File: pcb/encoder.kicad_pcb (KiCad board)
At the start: 2 copper layers, 65 x 56 mm, 7 parts, among them J1 GPIO

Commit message: snapshot...working on routing
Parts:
- added C1: 0.1uF, Capacitor_SMD:C_0603_1608Metric, F.Cu at (139.7, 59.0)
- added C2: 0.1uF, Capacitor_SMD:C_0603_1608Metric, F.Cu at (139.7, 74.5)
- added C3: 10uF, Capacitor_SMD:C_0805_2012Metric, F.Cu at (108.5, 53.0)
- added J2: Foot Switch, TerminalBlock_Phoenix:TerminalBlock_Phoenix_PT-1,5-4-5.0-H_1x04_P5.00mm_Horizontal, F.Cu at (157.5, 68.5)
- added J3: X, TerminalBlock_Phoenix:TerminalBlock_Phoenix_PT-1,5-4-5.0-H_1x04_P5.00mm_Horizontal, F.Cu at (113.0, 64.5)
- added J4: X', TerminalBlock_Phoenix:TerminalBlock_Phoenix_PT-1,5-4-5.0-H_1x04_P5.00mm_Horizontal, F.Cu at (157.5, 90.5)
- added J5: Y, TerminalBlock_Phoenix:TerminalBlock_Phoenix_PT-1,5-4-5.0-H_1x04_P5.00mm_Horizontal, F.Cu at (111.0, 91.5)
- added J6: Z, TerminalBlock_Phoenix:TerminalBlock_Phoenix_PT-1,5-4-5.0-H_1x04_P5.00mm_Horizontal, F.Cu at (133.0, 91.5)
- added R1: 4.7K, Resistor_SMD:R_0603_1608Metric, F.Cu at (150.7, 57.0)
- added R2: 4.7K, Resistor_SMD:R_0603_1608Metric, F.Cu at (128.2, 64.5)
- added R3: 4.7K, Resistor_SMD:R_0603_1608Metric, F.Cu at (128.2, 66.0)
- added R4: 4.7K, Resistor_SMD:R_0603_1608Metric, F.Cu at (128.2, 79.5)
- added R5: 4.7K, Resistor_SMD:R_0603_1608Metric, F.Cu at (128.2, 81.0)
- added R6: 4.7K, Resistor_SMD:R_0603_1608Metric, F.Cu at (139.7, 65.5)
- added R7: 4.7K, Resistor_SMD:R_0603_1608Metric, F.Cu at (139.7, 64.0)
- added R8: 4.7K, Resistor_SMD:R_0603_1608Metric, F.Cu at (139.7, 79.5)
- added R9: 4.7K, Resistor_SMD:R_0603_1608Metric, F.Cu at (139.7, 81.0)
- moved LS7466-S2 15.8 mm to (134.0, 78.9)
- moved LS7466-S1 10.1 mm to (134.0, 63.5)
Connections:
- LS7466-S1 pad 11: unconnected-(LS7466-S1-Ay-Pad11) -> Net-(J4-Pin_2)
- LS7466-S1 pad 12: unconnected-(LS7466-S1-By-Pad12) -> Net-(J4-Pin_3)
- LS7466-S1 pad 13: unconnected-(LS7466-S1-Zy-Pad13) -> GND
- LS7466-S1 pad 14: unconnected-(LS7466-S1-CEy-Pad14) -> +3.3V
- LS7466-S1 pad 16: unconnected-(LS7466-S1-VDD-Pad16) -> +3.3V
- LS7466-S1 pad 5: unconnected-(LS7466-S1-Ax-Pad5) -> Net-(J3-Pin_2)
- LS7466-S1 pad 6: unconnected-(LS7466-S1-Bx-Pad6) -> Net-(J3-Pin_3)
- LS7466-S1 pad 7: unconnected-(LS7466-S1-Zx-Pad7) -> GND
- LS7466-S1 pad 8: unconnected-(LS7466-S1-GND-Pad8) -> GND
- LS7466-S1 pad 9: unconnected-(LS7466-S1-CEx-Pad9) -> +3.3V
- LS7466-S2 pad 11: unconnected-(LS7466-S2-Ay-Pad11) -> Net-(J6-Pin_2)
- LS7466-S2 pad 12: unconnected-(LS7466-S2-By-Pad12) -> Net-(J6-Pin_3)
- LS7466-S2 pad 13: unconnected-(LS7466-S2-Zy-Pad13) -> GND
- LS7466-S2 pad 14: unconnected-(LS7466-S2-CEy-Pad14) -> +3.3V
- LS7466-S2 pad 16: unconnected-(LS7466-S2-VDD-Pad16) -> +3.3V
- LS7466-S2 pad 5: unconnected-(LS7466-S2-Ax-Pad5) -> Net-(J5-Pin_2)
- LS7466-S2 pad 6: unconnected-(LS7466-S2-Bx-Pad6) -> Net-(J5-Pin_3)
- LS7466-S2 pad 7: unconnected-(LS7466-S2-Zx-Pad7) -> GND
- LS7466-S2 pad 8: unconnected-(LS7466-S2-GND-Pad8) -> GND
- LS7466-S2 pad 9: unconnected-(LS7466-S2-CEx-Pad9) -> +3.3V
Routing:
- net GND: track 0.00 -> 226.8 mm, vias 0 -> 4
- net +3.3V: track 0.00 -> 72.1 mm
- net /GPIO9/SPI0.MISO: track 0.00 -> 48.3 mm
- net /GPIO10/SPI0.MOSI: track 0.00 -> 48.0 mm
- net /GPIO11/SPI0.SCLK: track 0.00 -> 47.9 mm
- net /GPIO8/SPI0.CE0: track 0.00 -> 36.7 mm
- net /GPIO7/SPI0.CE1: track 0.00 -> 22.1 mm
- net Net-(J5-Pin_2): track 0.00 -> 21.1 mm
- net /GPIO26: track 0.00 -> 18.3 mm
- net Net-(J5-Pin_3): track 0.00 -> 16.4 mm
- net Net-(J6-Pin_3): track 0.00 -> 16.1 mm
- net Net-(J6-Pin_2): track 0.00 -> 13.3 mm
- net Net-(J3-Pin_3): track 0.00 -> 2.77 mm
- net Net-(J3-Pin_2): track 0.00 -> 2.68 mm
- net +5V: track 0.00 -> 2.54 mm
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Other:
- outline, holes or cut-outs redrawn
- board text removed: "CAMERA (OPTIONAL)"
- board text removed: "DISPLAY (OPTIONAL)"
- board text removed: "PoE"

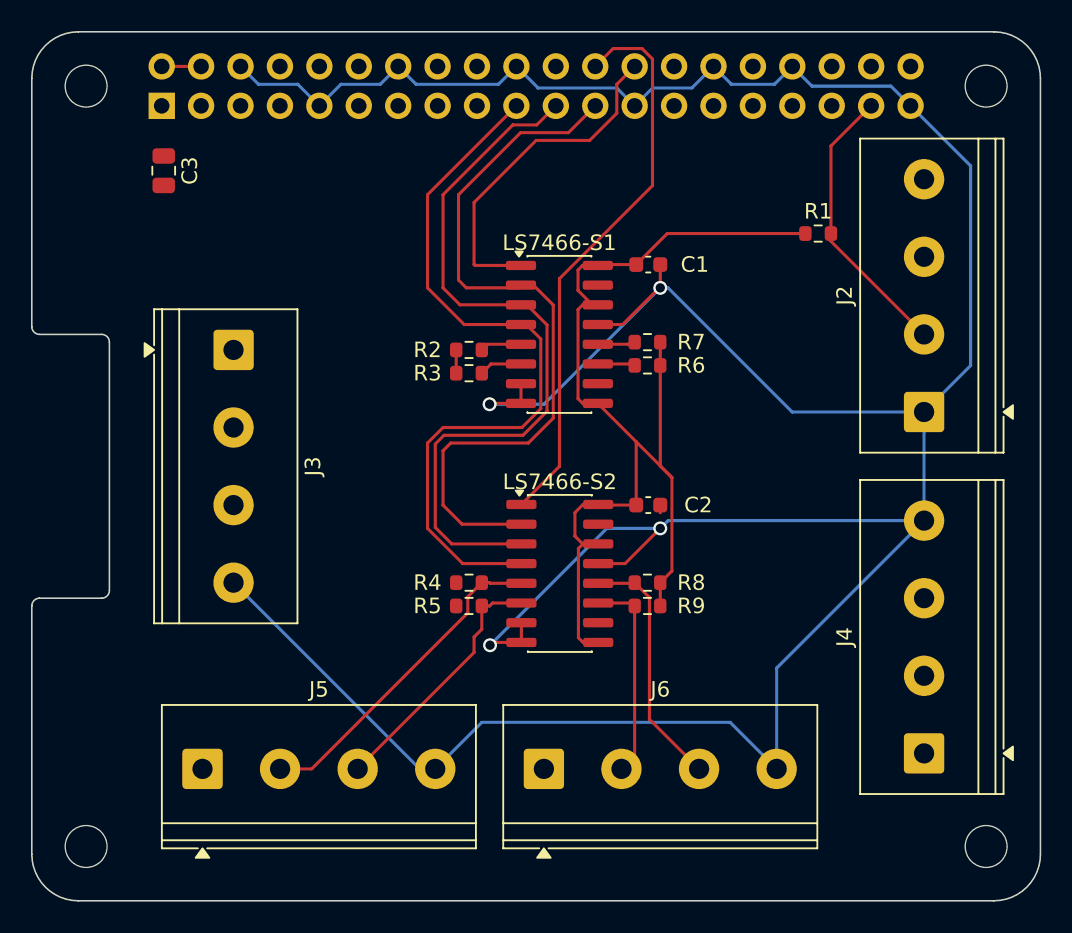
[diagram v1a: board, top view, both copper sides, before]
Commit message: route with ls74633 chips
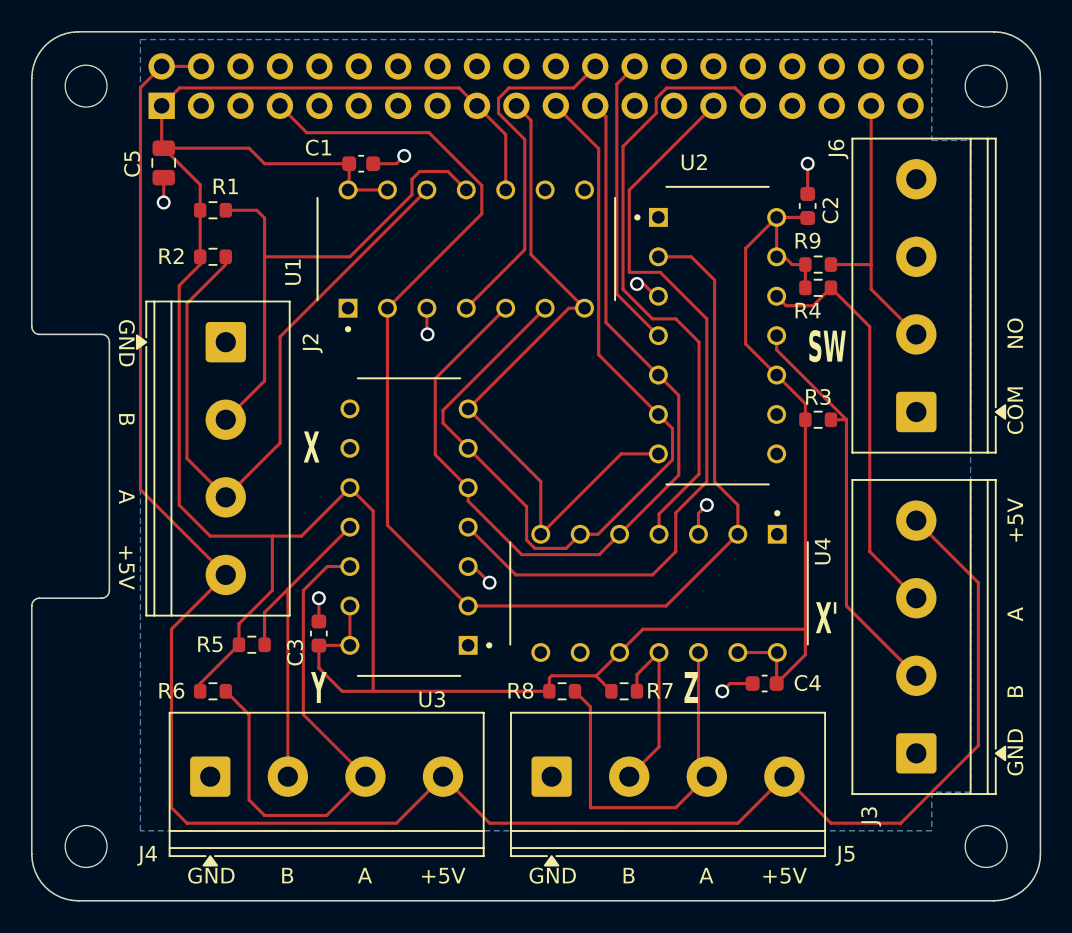
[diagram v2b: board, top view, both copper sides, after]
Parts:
- removed LS7466-S1, LS7466-S2: ~, Package_SO:SOIC-16_3.9x9.9mm_P1.27mm
- added C4: 0.1uF, Capacitor_SMD:C_0603_1608Metric, F.Cu at (147.2, 86.0)
- added C5: 10uF, Capacitor_SMD:C_0805_2012Metric, F.Cu at (108.5, 52.5)
- added U1: LS7366R, LS7366R:DIP762W45P254L1917H533Q14, F.Cu at (128.0, 58.0)
- added U2: LS7366R, LS7366R:DIP762W45P254L1917H533Q14, F.Cu at (144.2, 63.6)
- added U3: LS7366R, LS7366R:DIP762W45P254L1917H533Q14, F.Cu at (124.3, 75.9)
- added U4: LS7366R, LS7366R:DIP762W45P254L1917H533Q14, F.Cu at (140.4, 80.2)
- C3: value 10uF -> 0.1uF; footprint Capacitor_SMD:C_0805_2012Metric -> Capacitor_SMD:C_0603_1608Metric
- J2: value Foot Switch -> X
- J3: value X -> X'
- J4: value X' -> Y
- J5: value Y -> Z
- J6: value Z -> Foot Switch
- moved J3 51.1 mm to (157.0, 90.5), turned to 90 degrees
- moved J4 46.0 mm to (111.5, 92.0), turned to 0 degrees
- moved J2 45.2 mm to (112.5, 64.0), turned to -90 degrees
- moved R1 39.0 mm to (111.7, 55.5)
- moved R6 35.0 mm to (111.7, 86.5), turned to 0 degrees
- moved J6 33.2 mm to (157.0, 68.5), turned to 90 degrees
- moved C3 31.5 mm to (118.5, 82.8), turned to 90 degrees
- moved R4 29.4 mm to (150.7, 60.5)
- moved R9 24.6 mm to (150.7, 59.0), turned to 0 degrees
- moved R3 22.7 mm to (150.7, 69.0)
- moved R7 22.5 mm to (138.2, 86.5), turned to 0 degrees
- moved J5 22.5 mm to (133.5, 92.0)
- moved C2 21.8 mm to (150.0, 55.2), turned to 90 degrees
- moved C1 19.6 mm to (121.2, 52.5)
- moved R2 17.6 mm to (111.7, 58.5)
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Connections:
- C3 pad 1: +3V3 -> +3.3V
- J1 pad 1: +3V3 -> +3.3V
- J1 pad 17: +3V3 -> +3.3V
- J2 pad 2: /GPIO26 -> Net-(J2-Pin_2)
- J2 pad 3: unconnected-(J2-Pin_3-Pad3) -> Net-(J2-Pin_3)
- J2 pad 4: unconnected-(J2-Pin_4-Pad4) -> +5V
- J6 pad 1: +5V -> GND
- J6 pad 2: Net-(J6-Pin_2) -> /GPIO26
- J6 pad 3: Net-(J6-Pin_3) -> unconnected-(J6-Pin_3-Pad3)
- J6 pad 4: GND -> unconnected-(J6-Pin_4-Pad4)
- R1 pad 2: /GPIO26 -> Net-(J2-Pin_2)
- R2 pad 2: Net-(J3-Pin_2) -> Net-(J2-Pin_3)
- R3 pad 2: Net-(J3-Pin_3) -> Net-(J3-Pin_2)
- R4 pad 2: Net-(J5-Pin_2) -> Net-(J3-Pin_3)
- R5 pad 2: Net-(J5-Pin_3) -> Net-(J4-Pin_2)
- R6 pad 2: Net-(J4-Pin_2) -> Net-(J4-Pin_3)
- R7 pad 2: Net-(J4-Pin_3) -> Net-(J5-Pin_2)
- R8 pad 2: Net-(J6-Pin_3) -> Net-(J5-Pin_3)
- R9 pad 2: Net-(J6-Pin_2) -> /GPIO26
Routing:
- net GND: track 226.8 -> 16.7 mm, vias 4 -> 9
- net +5V: track 2.54 -> 130.2 mm
- net +3.3V: track 72.1 -> 197.6 mm
- net /GPIO4/GPCLK0: track 0.00 -> 87.4 mm
- net /GPIO5: track 0.00 -> 50.3 mm
- net Net-(J2-Pin_3): track 0.00 -> 42.2 mm
- net /GPIO6: track 0.00 -> 39.9 mm
- net Net-(J2-Pin_2): track 0.00 -> 33.1 mm
- net Net-(J4-Pin_3): track 1.93 -> 33.9 mm
- net Net-(J3-Pin_2): track 2.68 -> 26.6 mm
- net Net-(J3-Pin_3): track 2.77 -> 26.5 mm
- net Net-(J4-Pin_2): track 2.14 -> 21.9 mm
- net Net-(J6-Pin_3): track 16.1 -> 0.00 mm
- net /GPIO8/SPI0.CE0: track 36.7 -> 22.9 mm
- net Net-(J6-Pin_2): track 13.3 -> 0.00 mm
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- added copper zone on B.Cu, net GND
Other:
- board text added: "+5V"
- board text added: "A"
- board text added: "B"
- board text added: "COM"
- board text added: "GND"
- board text added: "NO"
- board text added: "SW"
- board text added: "X"
- board text added: "X'"
- board text added: "Y"
- board text added: "Z"

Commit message: update hardware.md to match schematic
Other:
- board text added: "https://github.com/scottfeldman/closinuf"
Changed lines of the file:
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@@
+		)
+	)
+	(gr_text "https://github.com/scottfeldman/closinuf"
+		(at 148.5 89 0)
+		(layer "B.SilkS")
+		(effects
+			(font
+				(size 1 1)
+				(thickness 0.15)
+			)
+			(justify left bottom mirror)
 		)
 	)

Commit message: update BOM
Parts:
- moved C4 1.55 mm to (148.8, 86.0), turned to 0 degrees
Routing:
- net GND: track 16.7 -> 16.0 mm

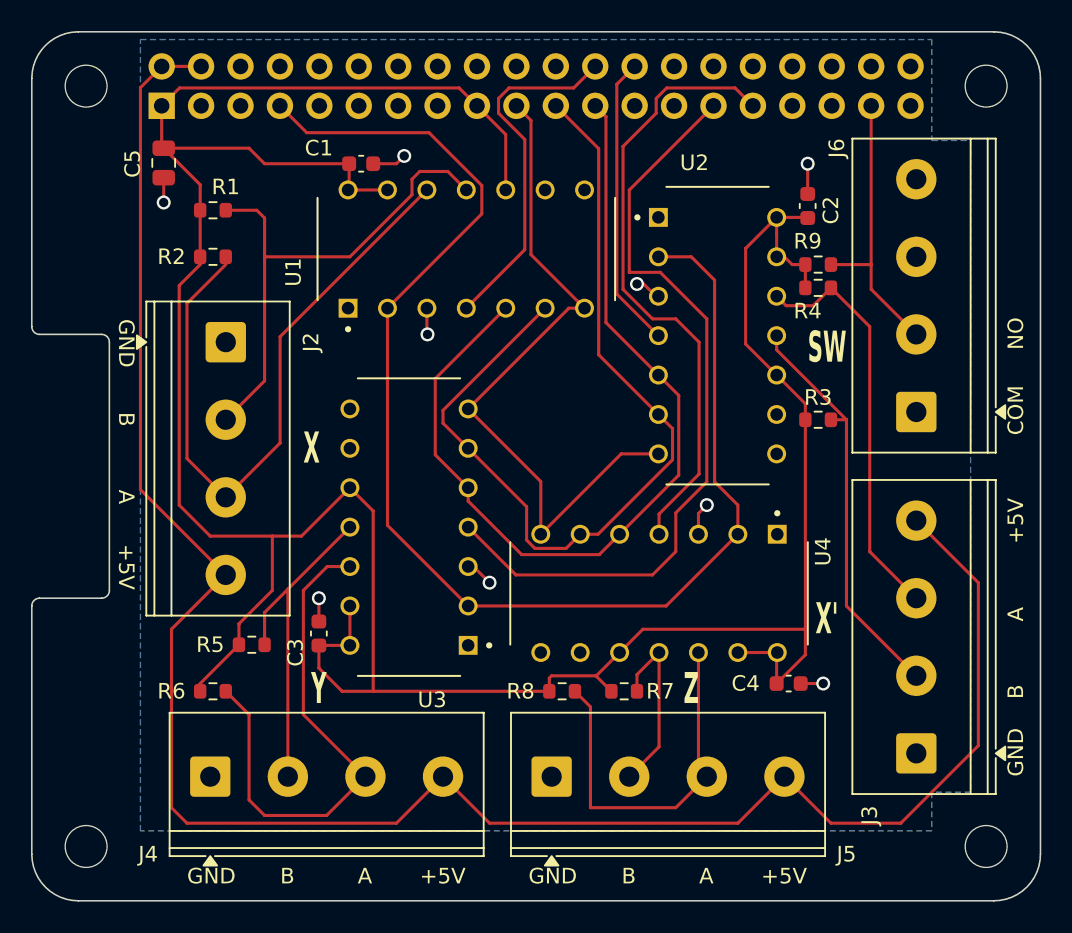
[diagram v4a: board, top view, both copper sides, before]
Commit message: move to thru-hole resistors/caps to save costs
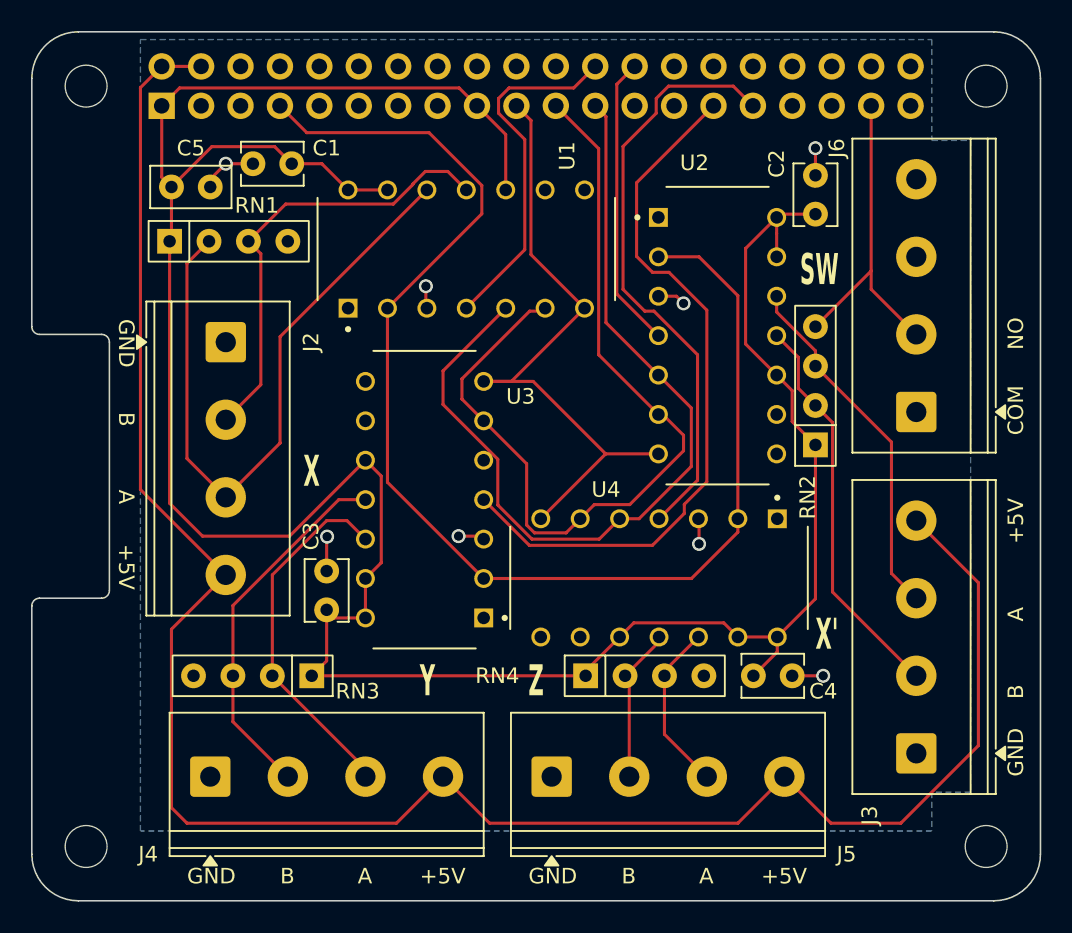
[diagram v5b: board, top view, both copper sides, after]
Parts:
- removed R1, R2, R3, R4, R5, R6, R7, R8, R9: 4.7K, Resistor_SMD:R_0603_1608Metric
- added RN1: 4.7K, Resistor_THT:R_Array_SIP4, F.Cu at (108.9, 57.5)
- added RN2: 4.7K, Resistor_THT:R_Array_SIP4, F.Cu at (150.5, 70.6)
- added RN3: 4.7K, Resistor_THT:R_Array_SIP4, F.Cu at (118.0, 85.5)
- added RN4: 4.7K, Resistor_THT:R_Array_SIP4, F.Cu at (135.7, 85.5)
- C1, C2, C3, C4: footprint Capacitor_SMD:C_0603_1608Metric -> Capacitor_THT:C_Disc_D3.8mm_W2.6mm_P2.50mm
- C5: footprint Capacitor_SMD:C_0805_2012Metric -> Capacitor_THT:C_Disc_D5.0mm_W2.5mm_P2.50mm
- moved C1 4.47 mm to (116.8, 52.5), turned to 180 degrees
- moved C4 2.33 mm to (146.5, 85.5)
- moved U3 2.03 mm to (125.3, 74.2)
- moved C5 1.63 mm to (109.0, 54.0), turned to 0 degrees
- moved C3 1.60 mm to (119.0, 81.2)
- moved U4 1.00 mm to (140.4, 79.2)
- moved C2 0.72 mm to (150.5, 55.8)
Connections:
- net /GPIO26 renamed FS
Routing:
- net +3.3V: track 197.6 -> 174.4 mm
- net Net-(J5-Pin_3): track 24.5 -> 11.0 mm
- net Net-(J4-Pin_3): track 33.9 -> 23.4 mm
- net Net-(J2-Pin_2): track 33.1 -> 29.2 mm
- net /GPIO5: track 50.3 -> 46.4 mm
- net Net-(J3-Pin_3): track 26.5 -> 23.2 mm
- net /GPIO4/GPCLK0: track 87.4 -> 84.6 mm
- net FS: track 18.5 -> 21.0 mm
- net /GPIO10/SPI0.MOSI: track 44.8 -> 42.4 mm
- net Net-(J4-Pin_2): track 21.9 -> 23.9 mm
- net Net-(J5-Pin_2): track 11.9 -> 10.0 mm
- net /GPIO6: track 39.9 -> 38.4 mm
- net /GPIO11/SPI0.SCLK: track 58.3 -> 56.9 mm
- net Net-(J2-Pin_3): track 42.2 -> 43.3 mm
- net /GPIO9/SPI0.MISO: track 57.8 -> 56.8 mm
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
